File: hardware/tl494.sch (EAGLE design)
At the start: 72 parts, among them IC1 TL494CN, K1 24V, Q1 2N5551, Q1I 8050, Q2 8550, Q2I 8050, Q3 8050, Q4 2SK4145, Q5 2SK4145

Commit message: minor update
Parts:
- R12: device rcl:R-EU_0207/10 -> rcl:R-EU_0207/5V
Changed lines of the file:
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@@
 <?xml version="1.0" encoding="utf-8"?>
 <!DOCTYPE eagle SYSTEM "eagle.dtd">
-<eagle version="9.4.2">
+<eagle version="9.1.3">
 <drawing>
 <settings>
@@
 <part name="R11" library="rcl" library_urn="urn:adsk.eagle:library:334" deviceset="R-EU_" device="0207/10" package3d_urn="urn:adsk.eagle:package:23491/2" value="10K"/>
 <part name="D1" library="diode" library_urn="urn:adsk.eagle:library:210" deviceset="1N4148" device="DO35-10" package3d_urn="urn:adsk.eagle:package:43344/2" value="1N4148"/>
-<part name="R12" library="rcl" library_urn="urn:adsk.eagle:library:334" deviceset="R-EU_" device="0207/10" package3d_urn="urn:adsk.eagle:package:23491/2" value="2K"/>
+<part name="R12" library="rcl" library_urn="urn:adsk.eagle:library:334" deviceset="R-EU_" device="0207/5V" package3d_urn="urn:adsk.eagle:package:23502/1" value="2K"/>
 <part name="C3" library="rcl" library_urn="urn:adsk.eagle:library:334" deviceset="C-EU" device="050-030X075" package3d_urn="urn:adsk.eagle:package:23640/1" value="0.1uF"/>
 <part name="GND6" library="dp_devices.v6" deviceset="SUPPLY_GND" device=""/>

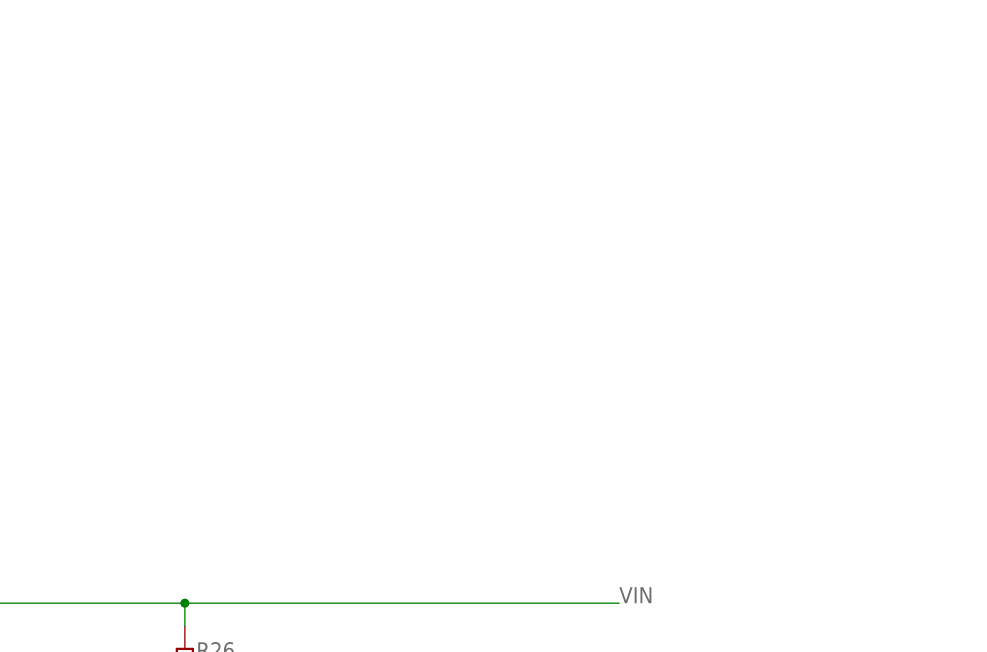
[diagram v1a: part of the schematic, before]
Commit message: added turn on latch circuit and gitignore
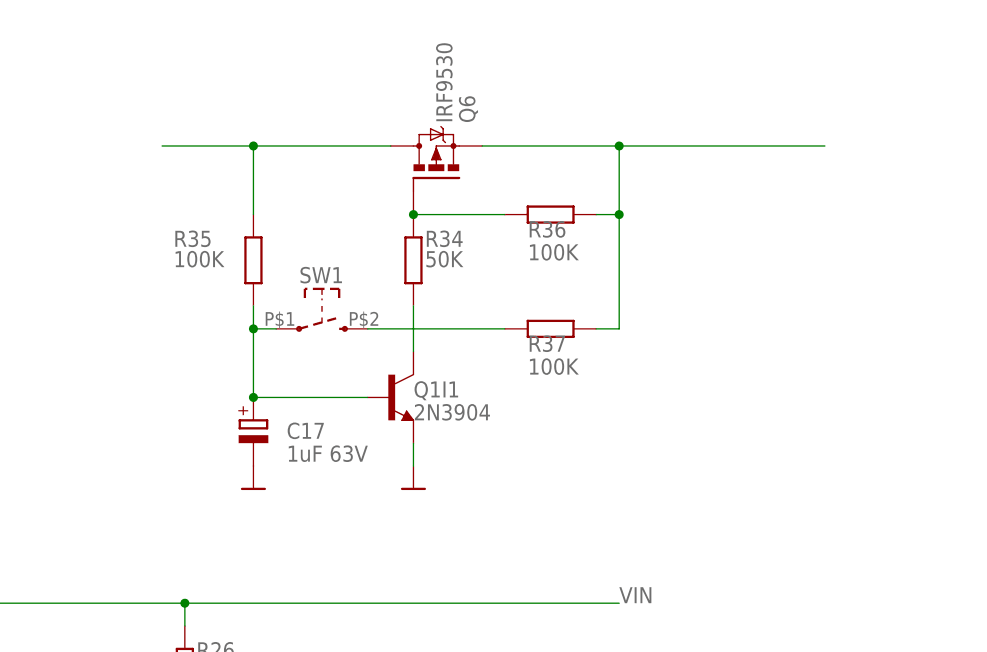
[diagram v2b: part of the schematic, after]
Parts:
- added C17: 1uF 63V, rcl:CPOL-EUE3.5-10
- added Q1I1: 2N3904, dp_devices.v6:TRANSISTOR_BJT_NPN-TO-92-EBC
- added Q6: IRF9530, transistor-power:IRF9530
- added R34: 50K, rcl:R-EU_0207/10
- added R35, R36, R37: 100K, rcl:R-EU_0207/10
- added SW1: SW_MEMBRANE, dp_devices.v6:SW_MEMBRANE
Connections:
- new net N$29: Q6.S, R36.1, R37.1
- new net N$30: Q6.G, R34.2, R36.2
- new net N$31: Q1I1.C, R34.1
- new net N$32: Q6.D, R35.2
- new net N$33: C17.+, Q1I1.B, R35.1, SW1.1
- new net N$34: R37.2, SW1.2
- net GND: now also C17.-, Q1I1.E
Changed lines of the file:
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@@
 <?xml version="1.0" encoding="utf-8"?>
 <!DOCTYPE eagle SYSTEM "eagle.dtd">
-<eagle version="9.1.3">
+<eagle version="9.4.2">
 <drawing>
 <settings>
@@
 <part name="GND31" library="dp_devices.v6" deviceset="SUPPLY_GND" device=""/>
 <part name="GND32" library="dp_devices.v6" deviceset="SUPPLY_GND" device=""/>
+<part name="Q6" library="transistor-power" library_urn="urn:adsk.eagle:library:400" deviceset="IRF9530" device="" package3d_urn="urn:adsk.eagle:package:29484/3"/>
+<part name="R34" library="rcl" library_urn="urn:adsk.eagle:library:334" deviceset="R-EU_" device="0207/10" package3d_urn="urn:adsk.eagle:package:23491/2" value="50K"/>
+<part name="Q1I1" library="dp_devices.v6" deviceset="TRANSISTOR_BJT_NPN" device="-TO-92-EBC" value="2N3904"/>
+<part name="GND33" library="dp_devices.v6" deviceset="SUPPLY_GND" device=""/>
+<part name="R35" library="rcl" library_urn="urn:adsk.eagle:library:334" deviceset="R-EU_" device="0207/10" package3d_urn="urn:adsk.eagle:package:23491/2" value="100K"/>
+<part name="R36" library="rcl" library_urn="urn:adsk.eagle:library:334" deviceset="R-EU_" device="0207/10" package3d_urn="urn:adsk.eagle:package:23491/2" value="100K"/>
+<part name="R37" library="rcl" library_urn="urn:adsk.eagle:library:334" deviceset="R-EU_" device="0207/10" package3d_urn="urn:adsk.eagle:package:23491/2" value="100K"/>
+<part name="SW1" library="dp_devices.v6" deviceset="SW_MEMBRANE" device=""/>
+<part name="C17" library="rcl" library_urn="urn:adsk.eagle:library:334" deviceset="CPOL-EU" device="E3.5-10" package3d_urn="urn:adsk.eagle:package:23351/1" value="1uF 63V"/>
+<part name="GND34" library="dp_devices.v6" deviceset="SUPPLY_GND" device=""/>
 </parts>
 <sheets>
@@
 <instance part="GND31" gate="G$1" x="101.6" y="81.28" smashed="yes"/>
 <instance part="GND32" gate="G$1" x="109.22" y="81.28" smashed="yes"/>
+<instance part="Q6" gate="G$1" x="236.22" y="228.6" smashed="yes" rot="MR90">
+<attribute name="NAME" x="238.76" y="233.68" size="1.778" layer="95" rot="MR90"/>
+<attribute name="VALUE" x="236.22" y="233.68" size="1.778" layer="96" rot="MR90"/>
+</instance>
+<instance part="R34" gate="G$1" x="233.68" y="218.44" smashed="yes" rot="R90">
+<attribute name="NAME" x="234.95" y="219.9386" size="1.778" layer="95"/>
+<attribute name="VALUE" x="234.95" y="217.678" size="1.778" layer="96"/>
+</instance>
+<instance part="Q1I1" gate="Q" x="231.14" y="203.2" smashed="yes">
+<attribute name="NAME" x="233.68" y="203.2" size="1.778" layer="95"/>
+<attribute name="VALUE" x="233.68" y="200.66" size="1.778" layer="96"/>
+</instance>
+<instance part="GND33" gate="G$1" x="233.68" y="193.04" smashed="yes"/>
+<instance part="R35" gate="G$1" x="215.9" y="218.44" smashed="yes" rot="R90">
+<attribute name="NAME" x="207.01" y="219.9386" size="1.778" layer="95"/>
+<attribute name="VALUE" x="207.01" y="217.678" size="1.778" layer="96"/>
+</instance>
+<instance part="R36" gate="G$1" x="248.92" y="223.52" smashed="yes" rot="R180">
+<attribute name="NAME" x="246.38" y="220.98" size="1.778" layer="95"/>
+<attribute name="VALUE" x="246.38" y="218.44" size="1.778" layer="96"/>
+</instance>
+<instance part="R37" gate="G$1" x="248.92" y="210.82" smashed="yes" rot="R180">
+<attribute name="NAME" x="246.38" y="208.28" size="1.778" layer="95"/>
+<attribute name="VALUE" x="246.38" y="205.74" size="1.778" layer="96"/>
+</instance>
+<instance part="SW1" gate="G$1" x="223.52" y="213.36" smashed="yes">
+<attribute name="NAME" x="220.98" y="215.9" size="1.778" layer="95" font="vector"/>
+</instance>
+<instance part="C17" gate="G$1" x="215.9" y="200.66" smashed="yes">
+<attribute name="NAME" x="219.583" y="198.6026" size="1.778" layer="95"/>
+<attribute name="VALUE" x="219.583" y="196.0626" size="1.778" layer="96"/>
+</instance>
+<instance part="GND34" gate="G$1" x="215.9" y="193.04" smashed="yes"/>
 </instances>
 <busses>
@@
 <wire x1="109.22" y1="88.9" x2="109.22" y2="83.82" width="0.1524" layer="91"/>
 <pinref part="GND32" gate="G$1" pin="GND"/>
+</segment>
+<segment>
+<pinref part="Q1I1" gate="Q" pin="E"/>
+<pinref part="GND33" gate="G$1" pin="GND"/>
+<wire x1="233.68" y1="195.58" x2="233.68" y2="198.12" width="0.1524" layer="91"/>
+</segment>
+<segment>
+<pinref part="C17" gate="G$1" pin="-"/>
+<pinref part="GND34" gate="G$1" pin="GND"/>
 </segment>
 </net>
@@
 </segment>
 </net>
+<net name="N$29" class="0">
+<segment>
+<pinref part="Q6" gate="G$1" pin="S"/>
+<wire x1="241.3" y1="231.14" x2="256.54" y2="231.14" width="0.1524" layer="91"/>
+<pinref part="R36" gate="G$1" pin="1"/>
+<wire x1="256.54" y1="231.14" x2="279.4" y2="231.14" width="0.1524" layer="91"/>
+<wire x1="254" y1="223.52" x2="256.54" y2="223.52" width="0.1524" layer="91"/>
+<wire x1="256.54" y1="223.52" x2="256.54" y2="231.14" width="0.1524" layer="91"/>
+<junction x="256.54" y="231.14"/>
+<wire x1="256.54" y1="223.52" x2="256.54" y2="210.82" width="0.1524" layer="91"/>
+<junction x="256.54" y="223.52"/>
+<pinref part="R37" gate="G$1" pin="1"/>
+<wire x1="256.54" y1="210.82" x2="254" y2="210.82" width="0.1524" layer="91"/>
+</segment>
+</net>
+<net name="N$30" class="0">
+<segment>
+<pinref part="Q6" gate="G$1" pin="G"/>
+<pinref part="R34" gate="G$1" pin="2"/>
+<pinref part="R36" gate="G$1" pin="2"/>
+<wire x1="243.84" y1="223.52" x2="233.68" y2="223.52" width="0.1524" layer="91"/>
+<junction x="233.68" y="223.52"/>
+</segment>
+</net>
+<net name="N$31" class="0">
+<segment>
+<pinref part="R34" gate="G$1" pin="1"/>
+<pinref part="Q1I1" gate="Q" pin="C"/>
+<wire x1="233.68" y1="208.28" x2="233.68" y2="213.36" width="0.1524" layer="91"/>
+</segment>
+</net>
+<net name="N$32" class="0">
+<segment>
+<pinref part="Q6" gate="G$1" pin="D"/>
+<wire x1="231.14" y1="231.14" x2="215.9" y2="231.14" width="0.1524" layer="91"/>
+<pinref part="R35" gate="G$1" pin="2"/>
+<wire x1="215.9" y1="231.14" x2="205.74" y2="231.14" width="0.1524" layer="91"/>
+<wire x1="215.9" y1="223.52" x2="215.9" y2="231.14" width="0.1524" layer="91"/>
+<junction x="215.9" y="231.14"/>
+</segment>
+</net>
+<net name="N$33" class="0">
+<segment>
+<pinref part="Q1I1" gate="Q" pin="B"/>
+<pinref part="R35" gate="G$1" pin="1"/>
+<wire x1="228.6" y1="203.2" x2="215.9" y2="203.2" width="0.1524" layer="91"/>
+<wire x1="215.9" y1="203.2" x2="215.9" y2="210.82" width="0.1524" layer="91"/>
+<wire x1="215.9" y1="210.82" x2="215.9" y2="213.36" width="0.1524" layer="91"/>
+<wire x1="215.9" y1="210.82" x2="218.44" y2="210.82" width="0.1524" layer="91"/>
+<junction x="215.9" y="210.82"/>
+<pinref part="SW1" gate="G$1" pin="1"/>
+<pinref part="C17" gate="G$1" pin="+"/>
+<junction x="215.9" y="203.2"/>
+</segment>
+</net>
+<net name="N$34" class="0">
+<segment>
+<pinref part="R37" gate="G$1" pin="2"/>
+<wire x1="243.84" y1="210.82" x2="228.6" y2="210.82" width="0.1524" layer="91"/>
+<pinref part="SW1" gate="G$1" pin="2"/>
+</segment>
+</net>
